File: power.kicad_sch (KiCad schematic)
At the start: 12 parts, among them J4 USB_C_Receptacle_USB2.0, J5 Conn_01x05, U4 TPS5430DDA, U6 XC6206P332MR, U7 SRV05-4

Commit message: continue with the phys, add debug, hook more up
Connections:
- net +5V: no longer J4.A4 (VBUS), J4.A9 (VBUS), J4.B4 (VBUS), J4.B9 (VBUS), U7.5 (VBUS)
- new net VBUS: J4.A4 (VBUS), J4.A9 (VBUS), J4.B4 (VBUS), J4.B9 (VBUS), U7.5 (VBUS)
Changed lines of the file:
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@@
+	)
+	(junction
+		(at 71.12 27.94)
+		(diameter 0)
+		(color 0 0 0 0)
 	)
 	(junction
@@
 	)
 	(junction
-		(at 66.04 27.94)
-		(diameter 0)
-		(color 0 0 0 0)
-	)
-	(junction
 		(at 53.34 48.26)
 		(diameter 0)
@@
 	(wire
 		(pts
+			(xy 71.12 27.94) (xy 86.36 27.94)
+		)
+		(stroke
+			(width 0)
+			(type default)
+		)
+	)
+	(wire
+		(pts
 			(xy 55.88 121.92) (xy 55.88 127)
 		)
@@
 	(wire
 		(pts
-			(xy 66.04 27.94) (xy 86.36 27.94)
+			(xy 50.8 27.94) (xy 71.12 27.94)
 		)
 		(stroke
@@
 		(pts
 			(xy 50.8 35.56) (xy 55.88 35.56)
-		)
-		(stroke
-			(width 0)
-			(type default)
-		)
-	)
-	(wire
-		(pts
-			(xy 50.8 27.94) (xy 66.04 27.94)
 		)
 		(stroke
@@
 	)
 	(symbol
+		(lib_id "power:VBUS")
+		(at 71.12 27.94 0)
+		(unit 1)
+		(body_style 1)
+		(exclude_from_sim no)
+		(in_bom yes)
+		(on_board yes)
+		(in_pos_files yes)
+		(dnp no)
+		(fields_autoplaced yes)
+		(property "Reference" "#PWR030"
+			(at 71.12 31.75 0)
+			(hide yes)
+			(show_name no)
+			(do_not_autoplace no)
+			(effects
+				(font
+					(size 1.27 1.27)
+				)
+			)
+		)
+		(property "Value" "VBUS"
+			(at 71.12 22.86 0)
+			(show_name no)
+			(do_not_autoplace no)
+			(effects
+				(font
+					(size 1.27 1.27)
+				)
+			)
+		)
+		(property "Footprint" ""
+			(at 71.12 27.94 0)
+			(hide yes)
+			(show_name no)
+			(do_not_autoplace no)
+			(effects
+				(font
+					(size 1.27 1.27)
+				)
+			)
+		)
+		(property "Datasheet" ""
+			(at 71.12 27.94 0)
+			(hide yes)
+			(show_name no)
+			(do_not_autoplace no)
+			(effects
+				(font
+					(size 1.27 1.27)
+				)
+			)
+		)
+		(property "Description" "Power symbol creates a global label with name \"VBUS\""
+			(at 71.12 27.94 0)
+			(hide yes)
+			(show_name no)
+			(do_not_autoplace no)
+			(effects
+				(font
+					(size 1.27 1.27)
+				)
+			)
+		)
+		(pin "1"
+		)
+		(instances
+			(project "xmc-ecat-enet-twin"
+				(path "/f5c7c34d-e330-4aa5-be7e-80f0a3a977af/b245da37-9602-4b35-a25a-6ddbb1541ecf"
+					(reference "#PWR030")
+					(unit 1)
+				)
+			)
+		)
+	)
+	(symbol
 		(lib_id "power:GND")
 		(at 35.56 71.12 0)
@@
 					(unit 1)
 				)
-			)
-		)
-	)
-	(symbol
-		(lib_id "power:+5V")
-		(at 66.04 27.94 0)
-		(unit 1)
-		(body_style 1)
-		(exclude_from_sim no)
-		(in_bom yes)
-		(on_board yes)
-		(in_pos_files yes)
-		(dnp no)
-		(property "Reference" "#PWR022"
-			(at 66.04 31.75 0)
-			(hide yes)
-			(show_name no)
-			(do_not_autoplace no)
-			(effects
-				(font
-					(size 1.27 1.27)
-				)
-			)
-		)
-		(property "Value" "+5V"
-			(at 66.421 23.5458 0)
-			(show_name no)
-			(do_not_autoplace no)
-			(effects
-				(font
-					(size 1.27 1.27)
-				)
-			)
-		)
-		(property "Footprint" ""
-			(at 66.04 27.94 0)
-			(hide yes)
-			(show_name no)
-			(do_not_autoplace no)
-			(effects
-				(font
-					(size 1.27 1.27)
-				)
-			)
-		)
-		(property "Datasheet" ""
-			(at 66.04 27.94 0)
-			(hide yes)
-			(show_name no)
-			(do_not_autoplace no)
-			(effects
-				(font
-					(size 1.27 1.27)
-				)
-			)
-		)
-		(property "Description" ""
-			(at 66.04 27.94 0)
-			(hide yes)
-			(show_name no)
-			(do_not_autoplace no)
-			(effects
-				(font
-					(size 1.27 1.27)
-				)
-			)
-		)
-		(pin "1"
-		)
-		(instances
-			(project "xmc-ecat-enet-twin"
-				(path "/f5c7c34d-e330-4aa5-be7e-80f0a3a977af/b245da37-9602-4b35-a25a-6ddbb1541ecf"
-					(reference "#PWR022")
-					(unit 1)
-				)

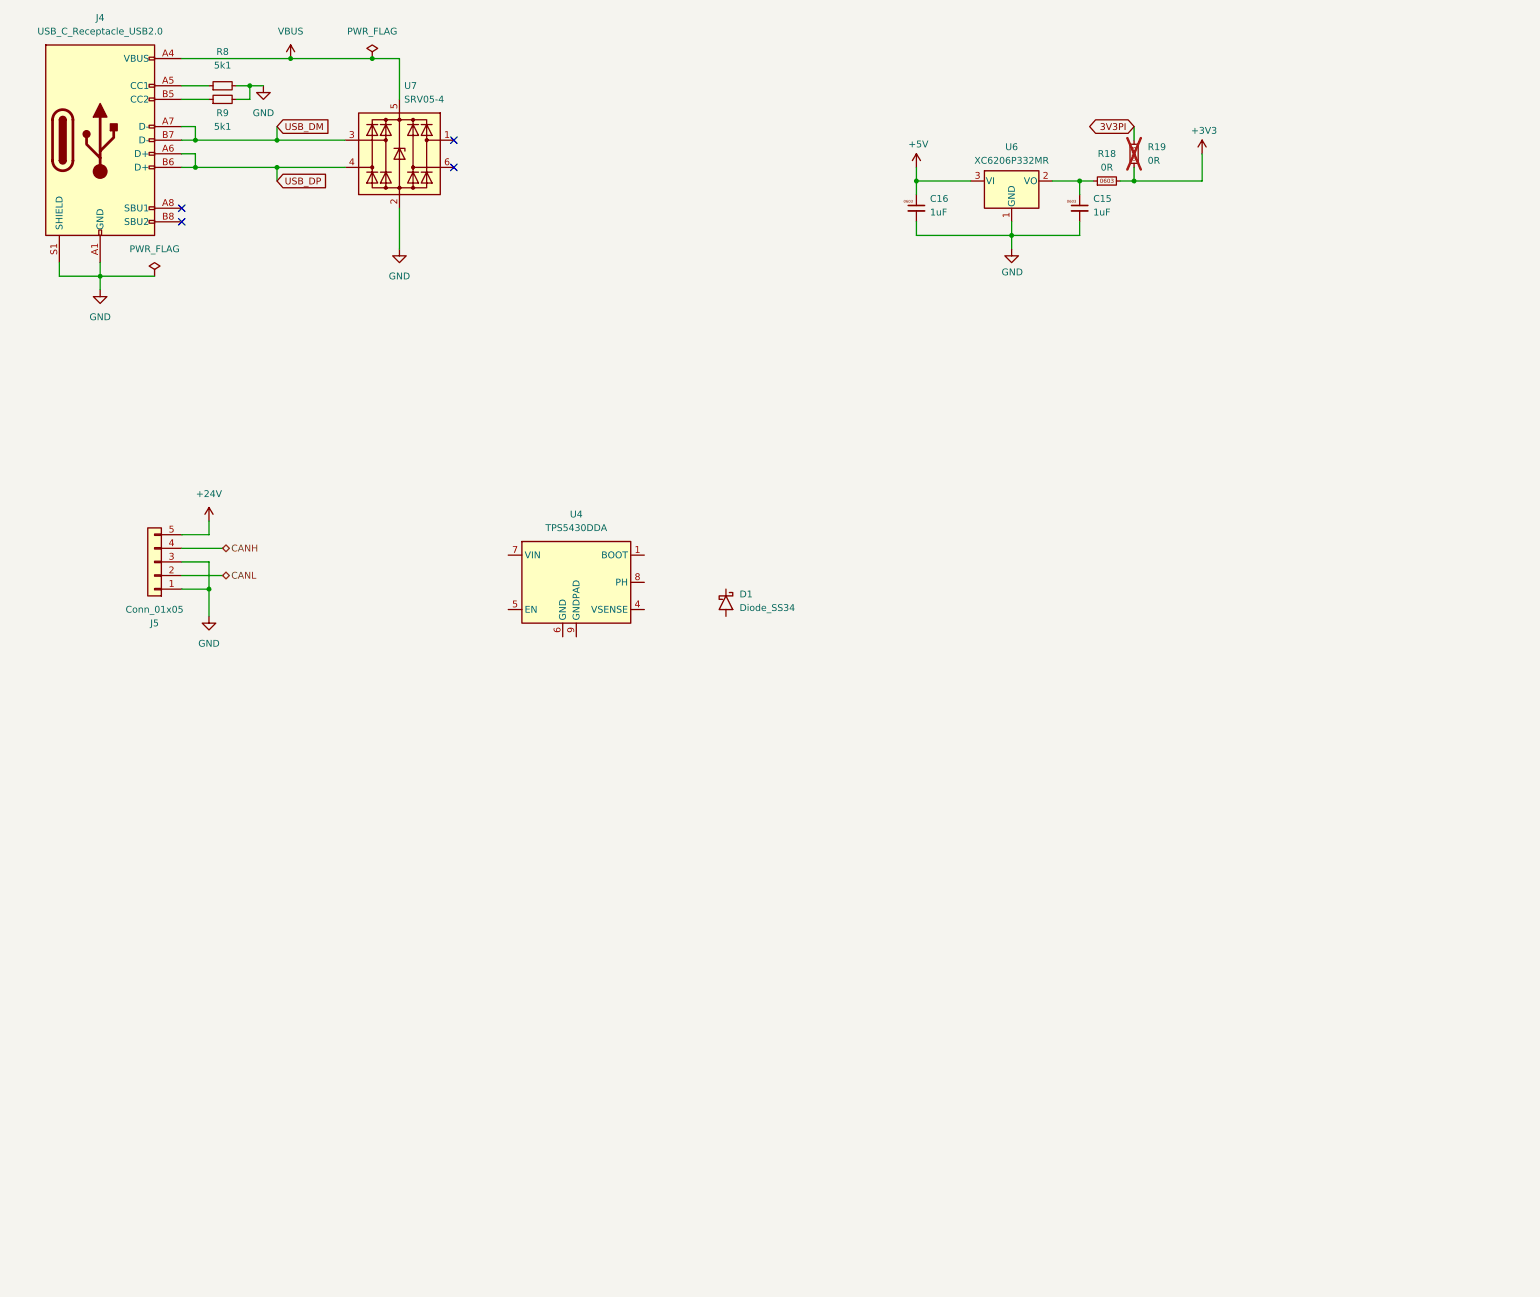
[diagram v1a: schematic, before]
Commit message: push forwards: clock muxing, filling in blanks
Finished off the ethernet section finally.
Sorted a solution to the 25M phy clocks required for ethercat
Connected CAN as per existing hardware (and fixed a bug in speed mode)
Sorted out bypassing for MCU
Added more thoughts on the external interfaces
Started on a 24V supply
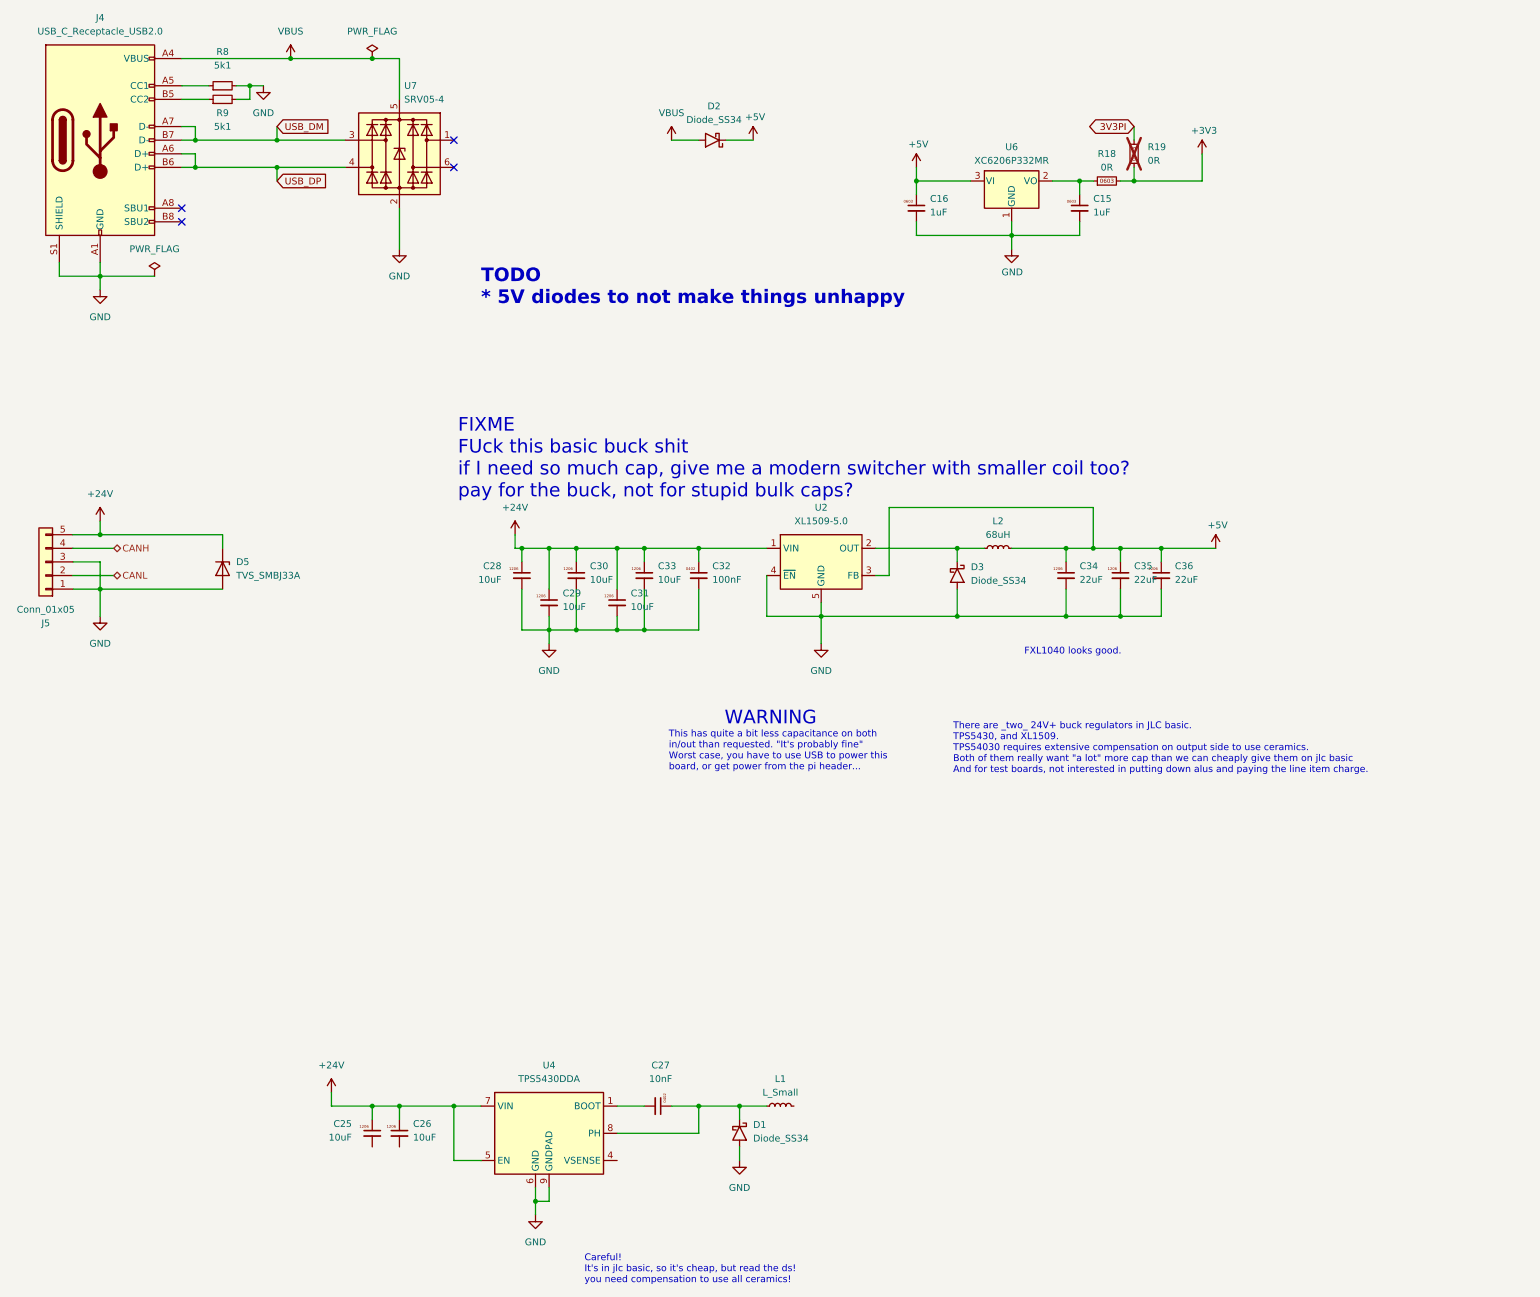
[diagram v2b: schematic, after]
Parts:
- added C25, C26, C28, C29, C30, C31, C33: 10uF, Capacitor_SMD:C_1206_3216Metric, symbol karl-atomic-basic:KC1206_10uF_50V
- added C27: 10nF, Capacitor_SMD:C_0402_1005Metric, symbol karl-atomic-basic:KC0402_10nF_50V
- added C32: 100nF, Capacitor_SMD:C_0402_1005Metric, symbol karl-atomic-basic:KC0402_100nF
- added C34, C35, C36: 22uF, Capacitor_SMD:C_1206_3216Metric, symbol karl-atomic-basic:KC1206_22uF_10V
- added D2, D3: Diode_SS34, Diode_SMD:D_SMA, symbol karl-atomic-basic:Diode_SS34
- added D5: TVS_SMBJ33A, Diode_SMD:D_SMB, symbol karl-atomic-basic:TVS_SMBJ33A
- added L1: L_Small, symbol Device:L_Small
- added L2: 68uH, Inductor_SMD:L_Changjiang_FXL1040, symbol Device:L_Small
- added U2: XL1509-5.0, Package_SO:SOIC-8_3.9x4.9mm_P1.27mm, symbol Regulator_Switching:XL1509-5.0
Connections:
- net +24V: now also U4.5 (EN), U4.7 (VIN), C25.1, C26.1, C28.1, C29.1, C30.1, C31.1, C32.1, C33.1, D5.1 (K), U2.1 (VIN)
- net +5V: now also C34.1, C35.1, C36.1, D2.1 (K), L2.2, U2.3 (FB)
- net GND: now also D1.2 (A), U4.6 (GND), U4.9 (GNDPAD), C28.2, C29.2, C30.2, C31.2, C32.2, C33.2, C34.2, C35.2, C36.2, D3.2 (A), D5.2 (A), U2.4 (~{EN}), U2.5 (GND), U2.6 (GND), U2.7 (GND), U2.8 (GND)
- net VBUS: now also D2.2 (A)
- net at U4.1 (BOOT): now also C27.2
- net at U4.8 (PH): now also D1.1 (K), C27.1, L1.1
- new net: D3.1 (K), L2.1, U2.2 (OUT)
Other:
- note added: "Careful! It's in jlc basic, so it's cheap, but read the ds! you need compensation to use all ceramics!"
- note added: "FIXME FUck this basic buck shit if I need so much cap, give me a modern switcher with smaller coil too? pay for the buck, not for stupid bulk caps?"
- note added: "FXL1040 looks good."
- note added: "TODO * 5V diodes to not make things unhappy"
- note added: "There are _two_ 24V+ buck regulators in JLC basic. TPS5430, and XL1509. TPS54030 requires extensive compensation on output side to use ceramics. Both of them really want "a lot" more cap than we can cheaply give them on jlc basic And for test boards, not interested in putting down alus and paying the line item charge."
- note added: "This has quite a bit less capacitance on both in/out than requested. "It's probably fine" Worst case, you have to use USB to power this board, or get power from the pi header..."
- note added: "WARNING"
- moved on the sheet: D1, J5, U4

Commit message: finish a 24V supply
went with a more modern one, plenty of room.  Should be pretty good now.
Went over and filled in a bunch of missing parts and things, cleaned up
as much as I could 0603 vs 0402 for most, updated some thigns to current
atomic part library.

still to go, the "pi" interface and some sort of spi/io interface?
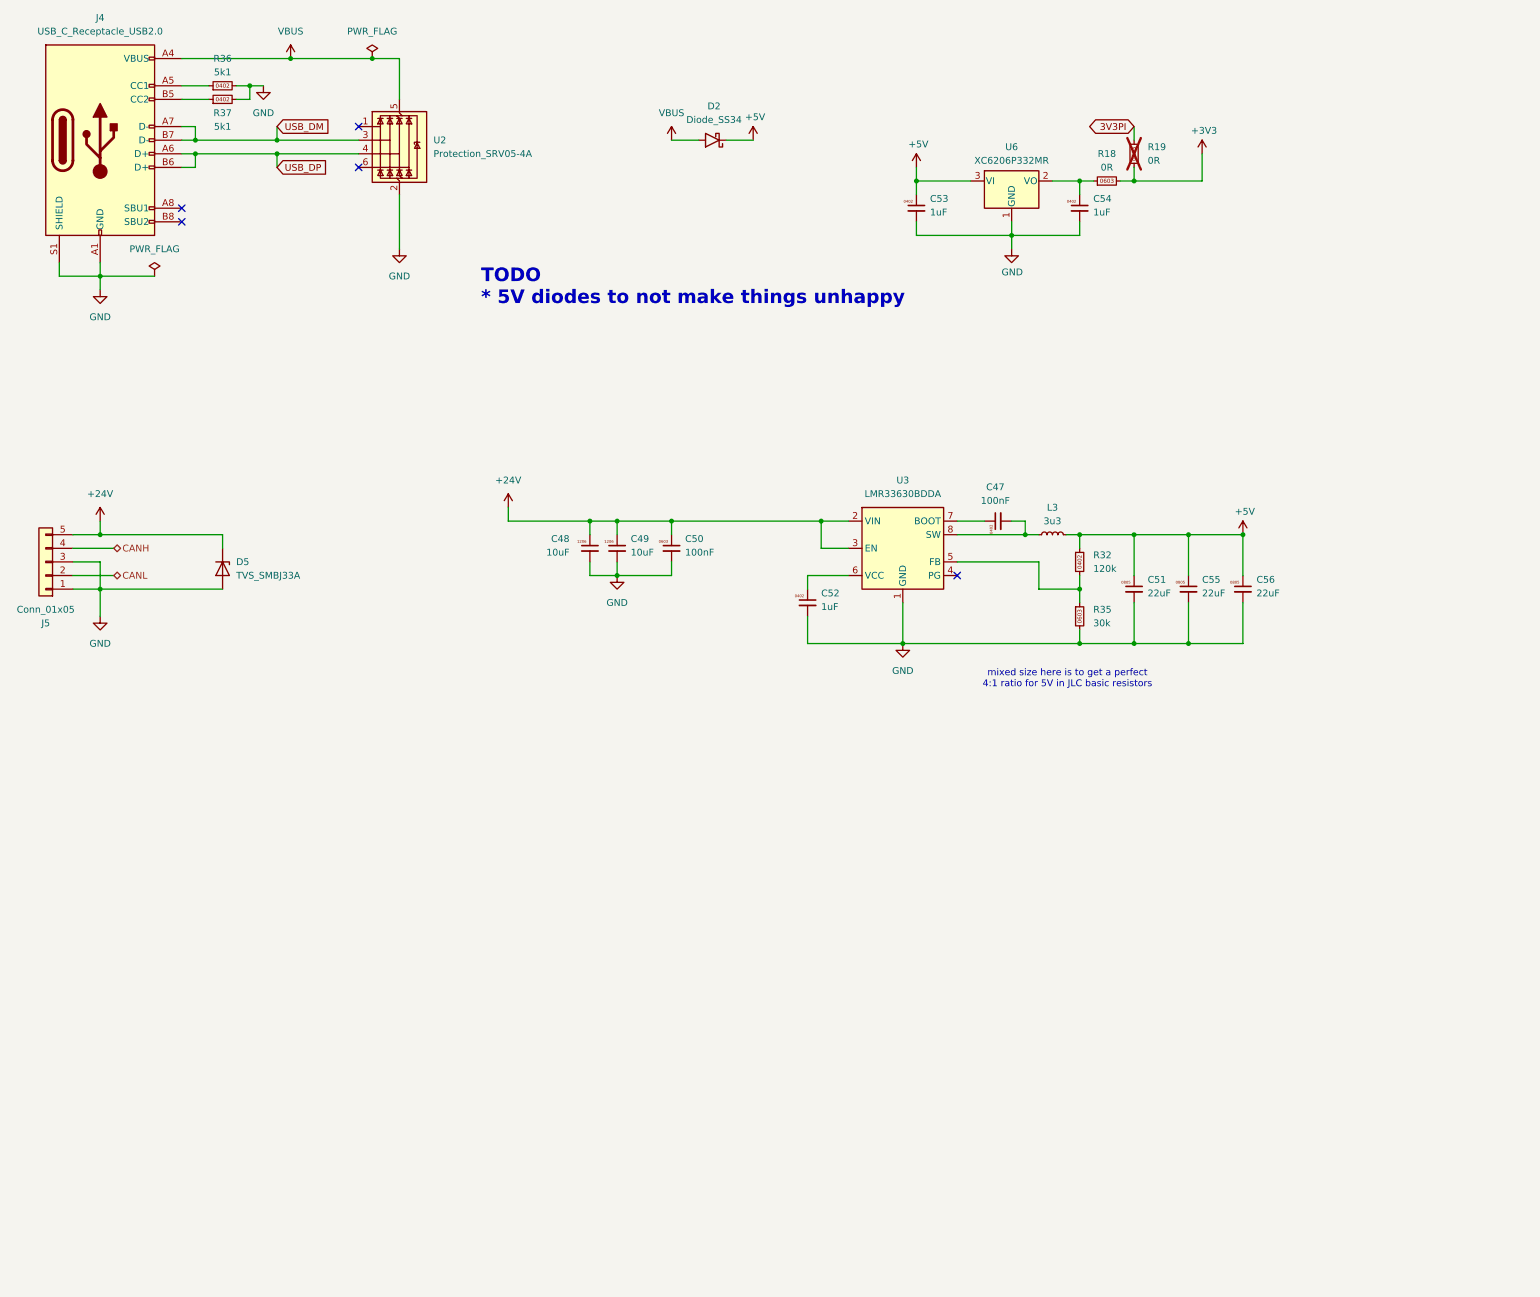
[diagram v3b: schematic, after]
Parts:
- removed C15, C16: 1uF, Capacitor_SMD:C_0603_1608Metric, symbol karl-atomic-basic:KC0603_1uF
- removed C25, C26, C28, C29, C30, C31, C33: 10uF, Capacitor_SMD:C_1206_3216Metric, symbol karl-atomic-basic:KC1206_10uF_50V
- removed C27: 10nF, Capacitor_SMD:C_0402_1005Metric, symbol karl-atomic-basic:KC0402_10nF_50V
- removed C32: 100nF, Capacitor_SMD:C_0402_1005Metric, symbol karl-atomic-basic:KC0402_100nF
- removed C34, C35, C36: 22uF, Capacitor_SMD:C_1206_3216Metric, symbol karl-atomic-basic:KC1206_22uF_10V
- removed D1, D3: Diode_SS34, Diode_SMD:D_SMA, symbol karl-atomic-basic:Diode_SS34
- removed L1: L_Small, symbol Device:L_Small
- removed L2: 68uH, Inductor_SMD:L_Changjiang_FXL1040, symbol Device:L_Small
- removed R8, R9: 5k1, Resistor_SMD:R_0603_1608Metric, symbol Device:R_Small
- removed U2: XL1509-5.0, Package_SO:SOIC-8_3.9x4.9mm_P1.27mm, symbol Regulator_Switching:XL1509-5.0
- removed U4: TPS5430DDA, Package_SO:TI_SO-PowerPAD-8_ThermalVias, symbol Regulator_Switching:TPS5430DDA
- removed U7: SRV05-4, Package_TO_SOT_SMD:SOT-23-6, symbol karl-parts:SRV05-4
- added C47: 100nF, Capacitor_SMD:C_0402_1005Metric, symbol karl-atomic-basic:KC0402_100nF
- added C48, C49: 10uF, Capacitor_SMD:C_1206_3216Metric, symbol karl-atomic-basic:KC1206_10uF_50V
- added C50: 100nF, Capacitor_SMD:C_0603_1608Metric, symbol karl-atomic-basic:KC0603_100nF
- added C51, C55, C56: 22uF, Capacitor_SMD:C_0805_2012Metric, symbol karl-atomic-basic:KC0805_22uF_25V
- added C52, C53, C54: 1uF, Capacitor_SMD:C_0402_1005Metric, symbol karl-atomic-basic:KC0402_1uF_25V
- added L3: 3u3, Inductor_SMD:L_Changjiang_FNR4020S, symbol Device:L_Small
- added R32: 120k, Resistor_SMD:R_0402_1005Metric, symbol karl-atomic-basic:KR0402_120k
- added R35: 30k, Resistor_SMD:R_0603_1608Metric, symbol karl-atomic-basic:KR0603_30k
- added R36, R37: 5k1, Resistor_SMD:R_0402_1005Metric, symbol karl-atomic-basic:KR0402_5k1
- added U2: Protection_SRV05-4A, Package_TO_SOT_SMD:SOT-23-6, symbol karl-atomic-basic:Protection_SRV05-4A
- added U3: LMR33630BDDA, Package_SO:Texas_HSOP-8-1EP_3.9x4.9mm_P1.27mm_ThermalVias, symbol Regulator_Switching:LMR33630BDDA
- J4: LCSC Part # (none) -> C2927038; jlc-basic 0 -> (none); jlcbasic (none) -> 0; lcsc# C2927038 -> (none)
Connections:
- net +24V: now also C48.1, C49.1, C50.1, U3.2 (VIN), U3.3 (EN)
- net +5V: now also C51.1, C53.1, C55.1, C56.1, L3.2, R32.1
- net GND: now also C48.2, C49.2, C50.2, C51.2, C52.2, C53.2, C54.2, C55.2, C56.2, R35.2, R36.2, R37.2, U2.2 (GND), U3.1 (GND), U3.9 (GND)
- net USB_DM: now also U2.3 (I/O2)
- net USB_DP: now also U2.4 (I/O3)
- net VBUS: now also U2.5 (VBUS)
- net at J4.A5 (CC1): now also R36.1
- net at J4.B5 (CC2): now also R37.1
- net at R18.1, U6.2 (VO): now also C54.1
- new net: C47.1, U3.7 (BOOT)
- new net: C47.2, L3.1, U3.8 (SW)
- new net: R32.2, R35.1, U3.5 (FB)
- new net: C52.1, U3.6 (VCC)
- no-connect marks 4 -> 5
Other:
- note added: "mixed size here is to get a perfect 4:1 ratio for 5V in JLC basic resistors"
- note removed: "Careful! It's in jlc basic, so it's cheap, but read the ds! you need compensation to use all ceramics!"
- note removed: "FIXME FUck this basic buck shit if I need so much cap, give me a modern switcher with smaller coil too? pay for the buck, not for stupid bulk caps?"
- note removed: "FXL1040 looks good."
- note removed: "There are _two_ 24V+ buck regulators in JLC basic. TPS5430, and XL1509. TPS54030 requires extensive compensation on output side to use ceramics. Both of them really want "a lot" more cap than we can cheaply give them on jlc basic And for test boards, not interested in putting down alus and paying the line item charge."
- note removed: "This has quite a bit less capacitance on both in/out than requested. "It's probably fine" Worst case, you have to use USB to power this board, or get power from the pi header..."
- note removed: "WARNING"
